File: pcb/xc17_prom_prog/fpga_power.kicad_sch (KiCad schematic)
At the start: 69 parts, among them J1 Conn_02x02_Odd_Even, J2 USB_B_Micro, U1 W25Q32JVSSIM, U2 LT3030, U3 ICE40HX1K-VQ100, U4 93LC56B, U5 FT2232HL, X1 12M

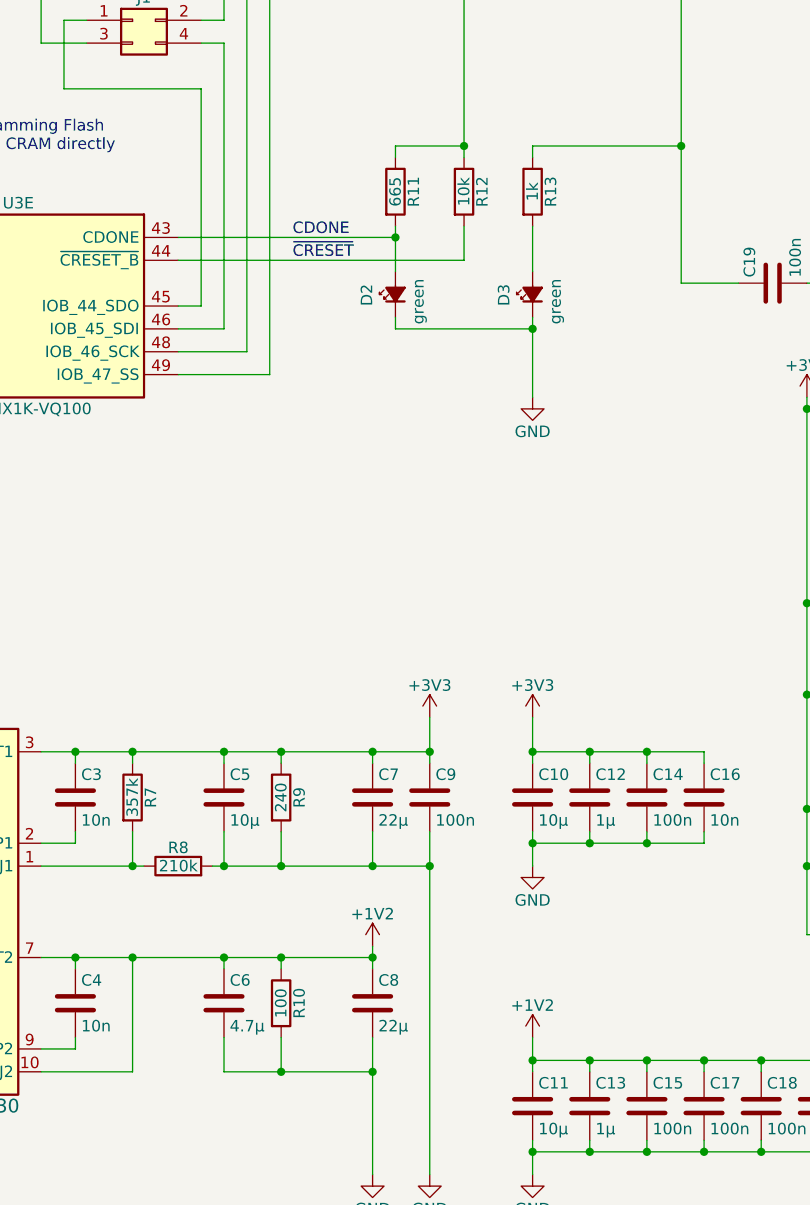
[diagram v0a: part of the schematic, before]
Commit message: Fix MOSFETs
 * Block MOSFET body diodes by placing two MOSFETs in anti series.
 * Connect PROM LED to pin header.
 * Add transistors to actively pull PROM VCC and VPP low.
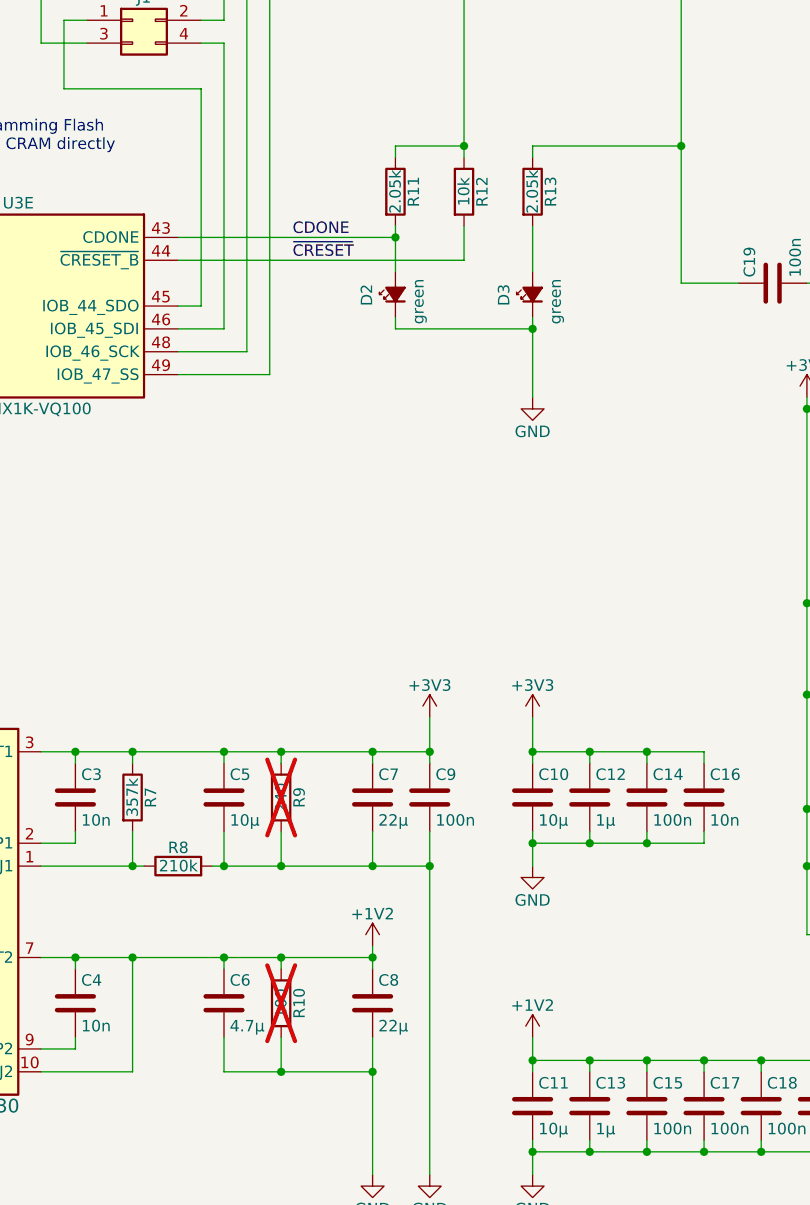
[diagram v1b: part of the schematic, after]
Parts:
- R10, R9: now not fitted; now left out of the parts list
- R11: value 665 -> 2.05k
- R13: value 1k -> 2.05k
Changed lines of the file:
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@@
 	(title_block
 		(title "XC17xxx PROM Programmer")
-		(date "2024-11-02")
-		(rev "0")
+		(date "2024-11-23")
+		(rev "1")
 		(company "CC-BY-SA-4.0 Michael Singer")
 		(comment 1 "https://github.com/msinger/xc17_prom_prog/")
@@
 		(at 92.71 147.32 0)
 		(unit 1)
-		(exclude_from_sim no)
-		(in_bom yes)
+		(exclude_from_sim yes)
+		(in_bom no)
 		(on_board yes)
-		(dnp no)
+		(dnp yes)
 		(property "Reference" "R9"
 			(at 94.742 147.32 90)
@@
 			)
 		)
-		(property "Value" "665"
+		(property "Value" "2.05k"
 			(at 105.41 80.01 90)
 			(effects
@@
 		(at 92.71 170.18 0)
 		(unit 1)
-		(exclude_from_sim no)
-		(in_bom yes)
+		(exclude_from_sim yes)
+		(in_bom no)
 		(on_board yes)
-		(dnp no)
+		(dnp yes)
 		(property "Reference" "R10"
 			(at 94.742 170.18 90)
@@
 			)
 		)
-		(property "Value" "1k"
+		(property "Value" "2.05k"
 			(at 120.65 80.01 90)
 			(effects

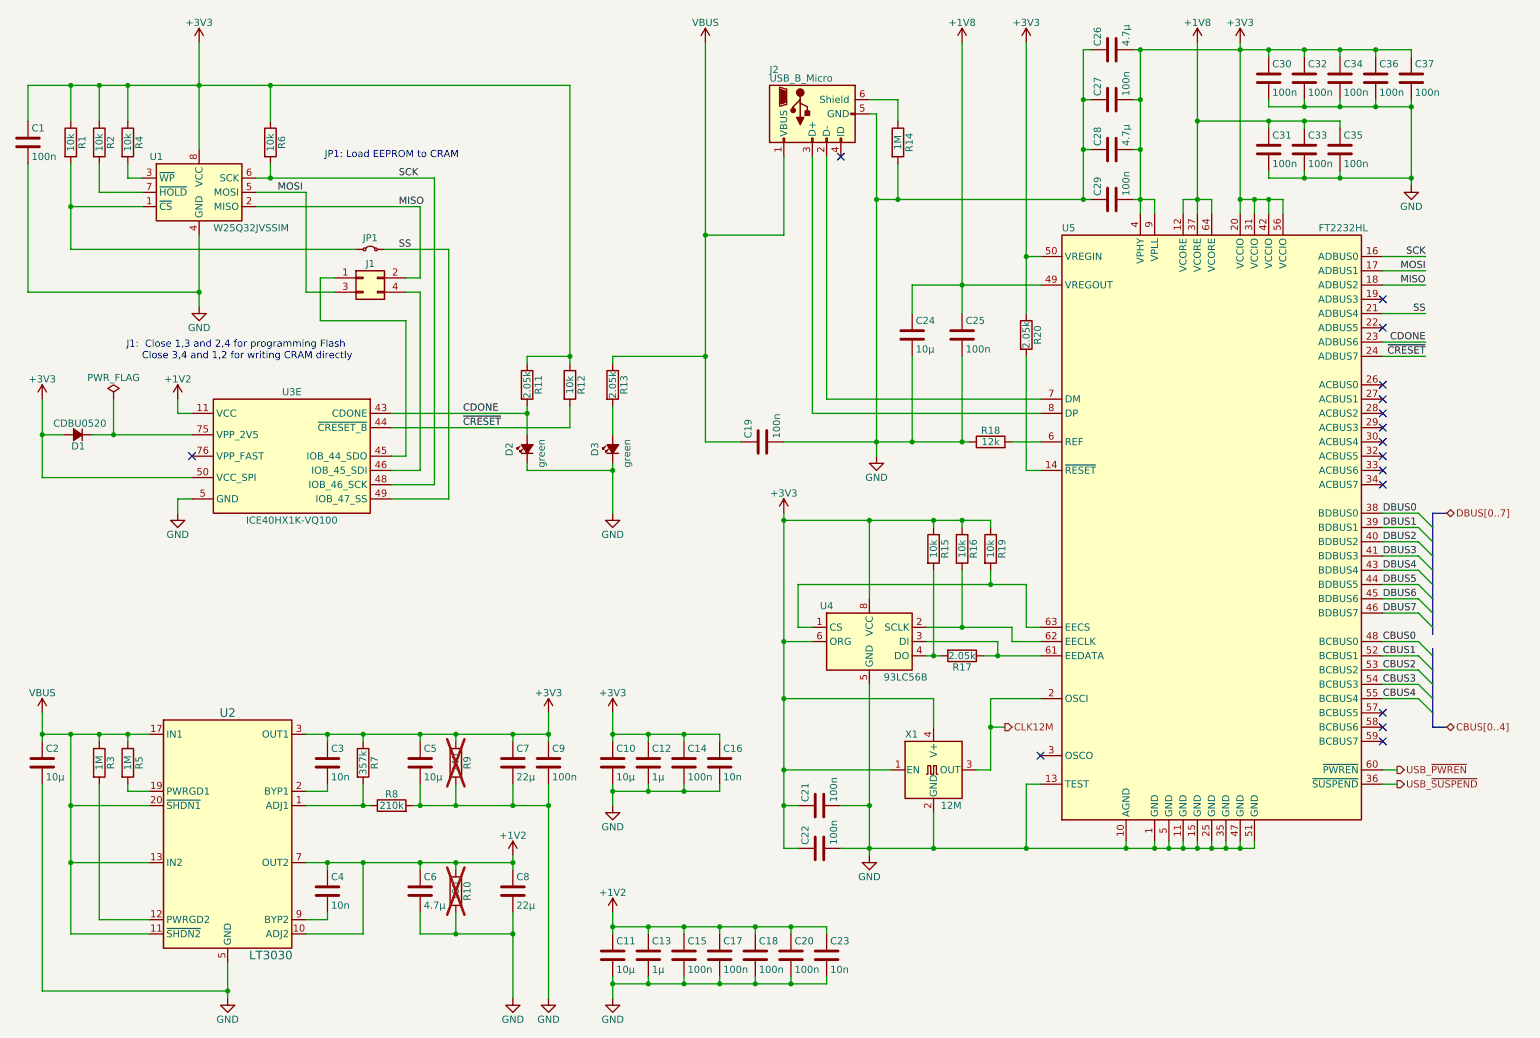
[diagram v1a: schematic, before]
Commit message: Implement more precise voltage controls
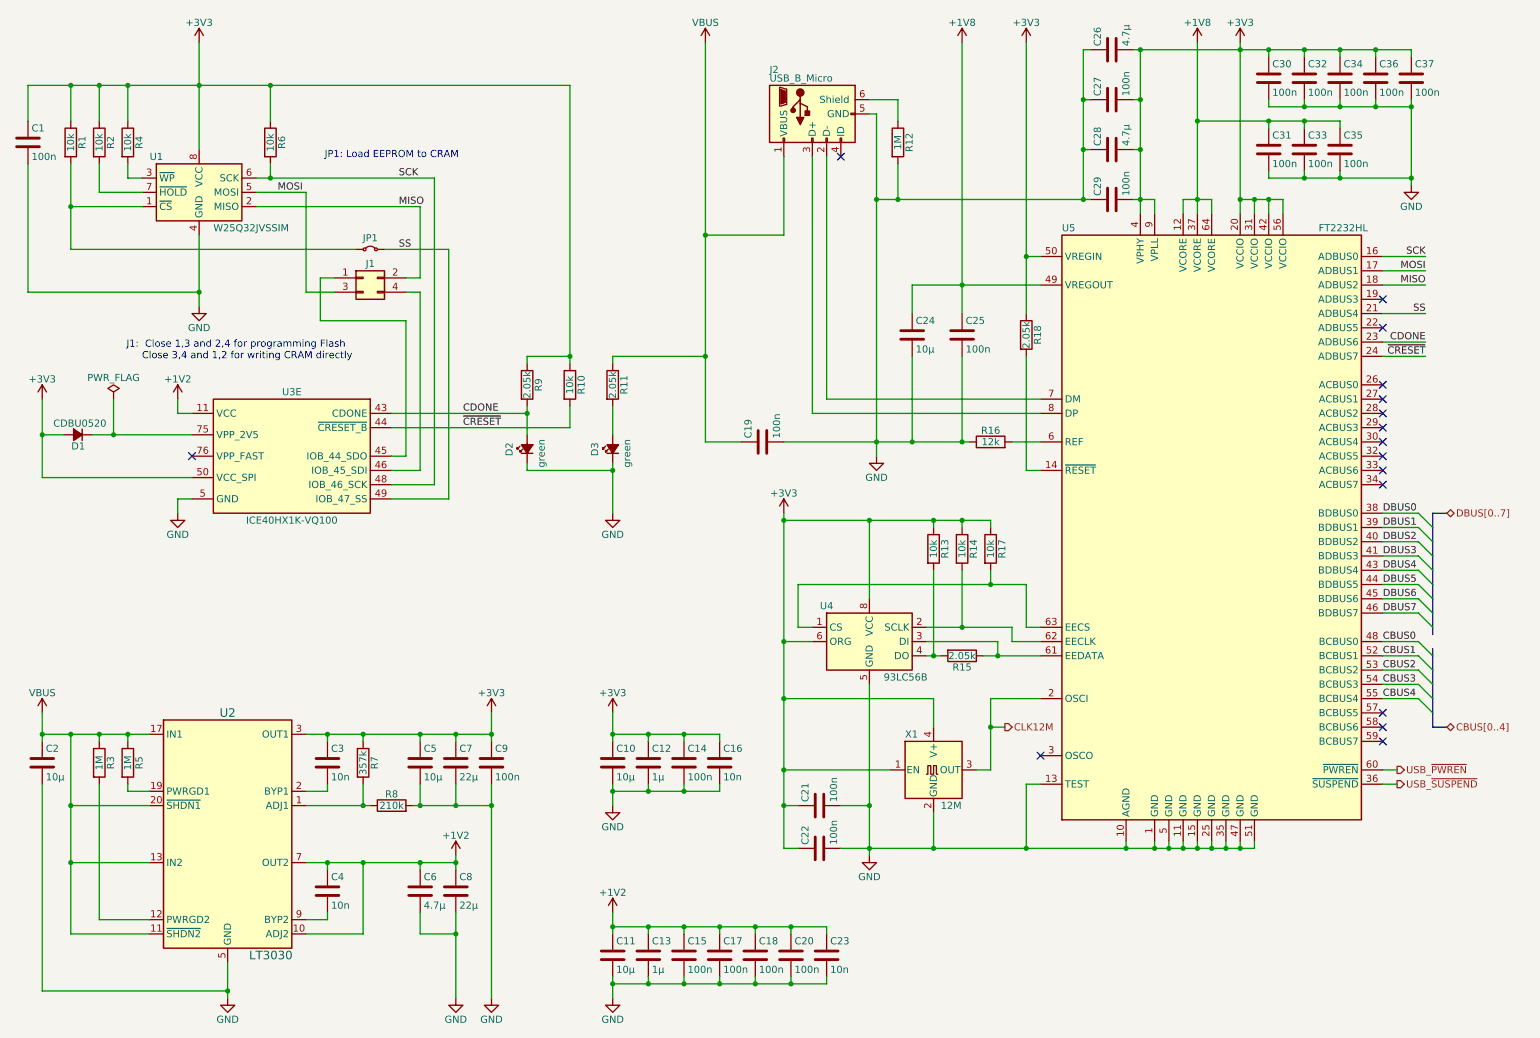
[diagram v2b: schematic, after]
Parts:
- removed R10: 100, Resistor_SMD:R_0603_1608Metric, symbol Device:R
- removed R9: 240, Resistor_SMD:R_0603_1608Metric, symbol Device:R
- renumbered R12 to R10, R13 to R11, R14 to R12, R15 to R13, R16 to R14, R17 to R15, R18 to R16, R19 to R17, R20 to R18, R11 to R9
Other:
- moved on the sheet: C7, C8, C9

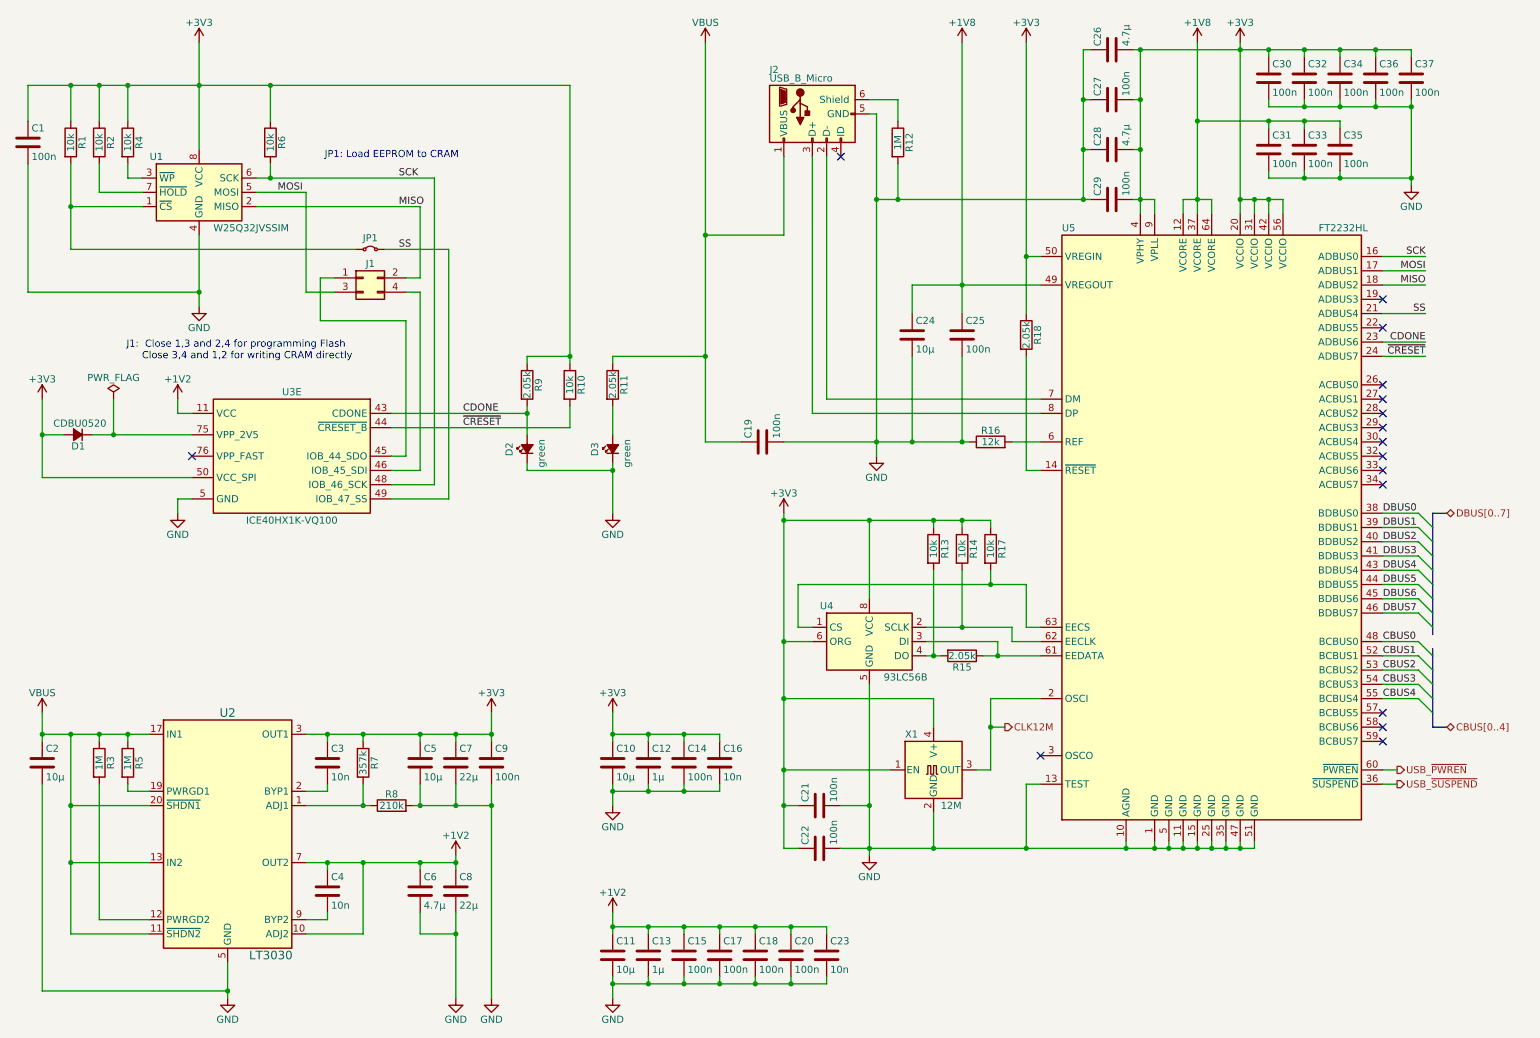
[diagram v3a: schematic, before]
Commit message: Migrate from HX1K to HX4K FPGA
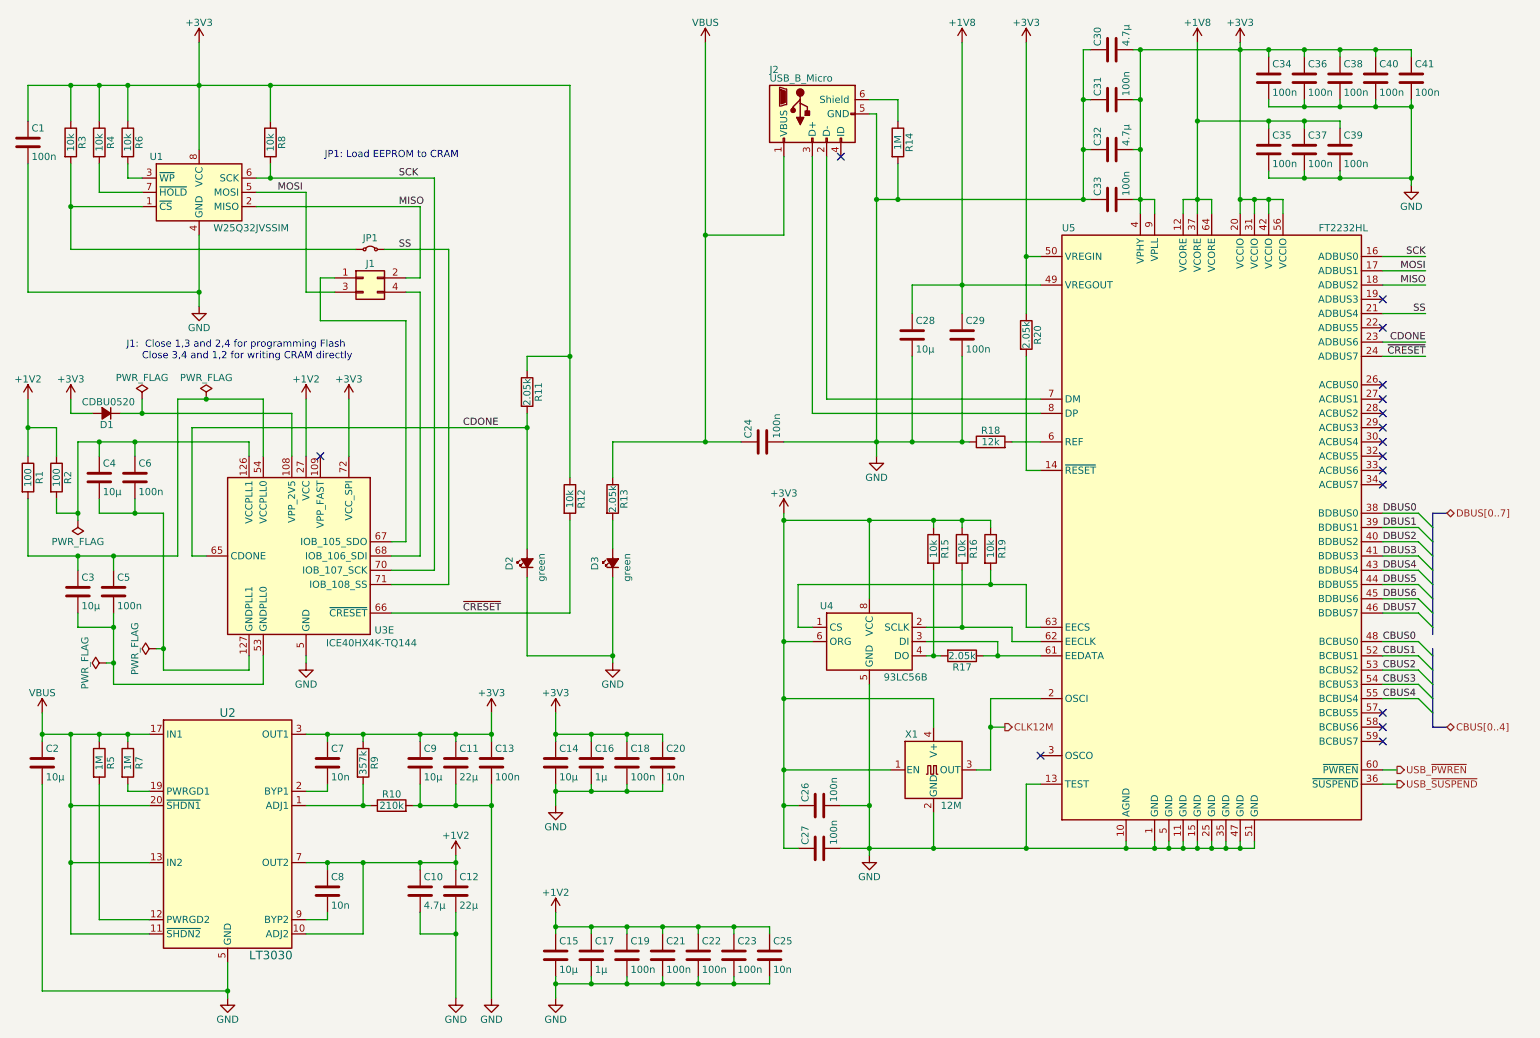
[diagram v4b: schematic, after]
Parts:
- removed U3: ICE40HX1K-VQ100, Package_QFP:VQFP-100_14x14mm_P0.5mm, symbol FPGA_Lattice_ICE40HX1K:ICE40HX1K-VQ100
- added C3, C4: 10µ, Capacitor_SMD:C_0603_1608Metric, symbol Device:C
- added C5, C6: 100n, Capacitor_SMD:C_0603_1608Metric, symbol Device:C
- added R1, R2: 100, Resistor_SMD:R_0603_1608Metric, symbol Device:R
- added U3: ICE40HX4K-TQ144, Package_QFP:TQFP-144_20x20mm_P0.5mm, symbol FPGA_Lattice:ICE40HX4K-TQ144
- renumbered C6 to C10, C7 to C11, C8 to C12, C9 to C13, C10 to C14, C11 to C15, C12 to C16, C13 to C17, C14 to C18, C15 to C19, C16 to C20, C17 to C21, C18 to C22, C20 to C23, C19 to C24, C23 to C25, C21 to C26, C22 to C27, C24 to C28, C25 to C29, C26 to C30, C27 to C31, C28 to C32, C29 to C33, C30 to C34, C31 to C35, C32 to C36, C33 to C37, C34 to C38, C35 to C39, C36 to C40, C37 to C41, C3 to C7, C4 to C8, C5 to C9, R8 to R10, R9 to R11, R10 to R12, R11 to R13, R12 to R14, R13 to R15, R14 to R16, R15 to R17, R16 to R18, R17 to R19, R18 to R20, R1 to R3, R2 to R4, R3 to R5, R4 to R6, R5 to R7, R6 to R8, R7 to R9
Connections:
- net +1V2: now also R1.1, R2.1, U3.111 (VCC), U3.27 (VCC), U3.40 (VCC), U3.92 (VCC)
- net +3V3: now also U3.72 (VCC_SPI)
- net CDONE: now also U3.65 (CDONE)
- net GND: now also U3.103 (GND), U3.13 (GND), U3.132 (GND), U3.14 (GND), U3.140 (GND), U3.5 (GND), U3.59 (GND), U3.69 (GND), U3.86 (GND)
- net SCK: now also U3.70 (IOB_107_SCK)
- net SS: now also U3.71 (IOB_108_SS)
- net ~{CRESET}: now also U3.66 (~{CRESET})
- net at J1.1 (Pin_1): now also U3.67 (IOB_105_SDO)
- net at J1.4 (Pin_4): now also U3.68 (IOB_106_SDI)
- net at D1.1 (K): now also U3.108 (VPP_2V5)
- new net: C3.1, C5.1, R1.2, U3.54 (VCCPLL0)
- new net: C3.2, C5.2, U3.53 (GNDPLL0)
- new net: C4.1, C6.1, R2.2, U3.126 (VCCPLL1)
- new net: C4.2, C6.2, U3.127 (GNDPLL1)
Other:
- moved on the sheet: C14, C15, C16, C17, C18, C19, C20, C21, C22, C23, C25, D1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
